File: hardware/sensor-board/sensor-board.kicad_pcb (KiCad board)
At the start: 2 copper layers, 65 x 76 mm, 76 parts, among them J1 HELM, J2 TACH, J3 PROBES, J4 RPi GPIO, J5 NMEA 2000, J6 LIGHTS, U1 ADS1115IDGSR, U2 ADS1115IDGSR, U3 EL817, U4 MCP2518FD, U5 ISO1044BD, U6 UA78L05, Y1 40MHz

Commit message: Sensor board: 5 V input (J7) that powers the Pi through the header
The Pi now runs from an external 12 V -> 5 V converter wired to J7 on the
board, through the header's 5 V pins (back-powering, 5 V +/-5 %, up to
2.5 A per the HAT guide); the board's 3V3 comes from the Pi as before.

An ideal diode sits in the way (TI LM74700-Q1 driving an IRLML0030): about
20 mV drop where a Schottky's 0.4 V would trip the Pi's undervoltage
warning. J7 wired backwards is blocked, and the Pi's USB-C can't push
current back into the converter. SMAJ5.0A clamp and 22 uF bulk on the
rail. Not protected: a converter failing with 12 V out (docs say to buy
one with output OVP).

The Pi's 5 V pins are in the header's top-left corner, boxed in by J1 and
a mounting hole, so J7 and the ideal diode go on a 35 x 12 mm tab above
the left half of the header (board now 65 x 88 overall). The router takes
an origin and off-board notches for that. Also:
- the 5 V current path routes wide first, sense pins and caps thin after;
  its run to the header goes on the bottom layer, where on top it walled
  off the header's GND pin 6 from the pour;
- vias keep their drill 0.25 mm off their own net's SMD pads (the router
  had put one on Q1's drain pad); none on the board now;
- BAT+ is documented as the dashboard switch's 12 V, the converter's feed.

ERC, DRC and parity: clean.

Co-Authored-By: Claude Opus 5.5 <noreply@anthropic.com>
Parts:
- added C19: 100n, sensor-board:C_0805_2012Metric_NoSilk, F.Cu at (126.6, 41.8)
- added C20: 100n, sensor-board:C_0805_2012Metric_NoSilk, F.Cu at (126.9, 45.4)
- added C21: 22u, sensor-board:C_1206_3216Metric_NoSilk, F.Cu at (129.6, 47.4)
- added D12: SMAJ5.0A, Diode_SMD:D_SMA, F.Cu at (132.6, 44.0)
- added J7: 5V IN, Connector_Phoenix_MC:PhoenixContact_MC_1,5_2-GF-3.81_1x02_P3.81mm_Horizontal_ThreadedFlange, F.Cu at (112.6, 46.7)
- added Q1: IRLML0030, Package_TO_SOT_SMD:SOT-23, F.Cu at (122.6, 47.8)
- added U7: LM74700-Q1, Package_TO_SOT_SMD:SOT-23-6, F.Cu at (122.7, 42.8)
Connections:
- J4 pad 2: unconnected-(J4-Pin_2-Pad2) -> +5V
- J4 pad 4: unconnected-(J4-Pin_4-Pad4) -> +5V
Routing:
- net +5V: track 0.00 -> 24.1 mm, vias 0 -> 1
- net /VIN: track 0.00 -> 23.8 mm
- net /N2K_GND: track 23.1 -> 32.3 mm, vias 2 -> 0
- net +3V3: track 190.5 -> 198.2 mm, vias 21 -> 19
- net /IDEAL_G: track 0.00 -> 3.77 mm, vias 0 -> 2
- net /N2K_L: track 19.7 -> 23.2 mm, vias 7 -> 6
- net GND: track 19.2 -> 21.3 mm, vias 36 -> 40
- net /N2K_H: track 26.7 -> 28.4 mm
- net /VCAP: track 0.00 -> 1.30 mm
- net /N2K_TERM: track 5.06 -> 6.19 mm, vias 0 -> 2
- net /LIGHT_DAT1: track 63.5 -> 64.5 mm
- net /CAN_INT: track 55.5 -> 56.5 mm
- net /LIGHT_DAT2: track 37.3 -> 38.3 mm
- net /N2K_5V: track 12.2 -> 13.0 mm
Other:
- board size 65 x 76 mm -> 65 x 88 mm
- board text added: "+5V"
- board text added: "5V IN: J7, converter at 5.1V"
- board text added: "BAT+: dashboard 12V, 1A fuse"
- board text added: "J7 5V IN"
- board text removed: "BAT+: +12V always on, 1A fuse"

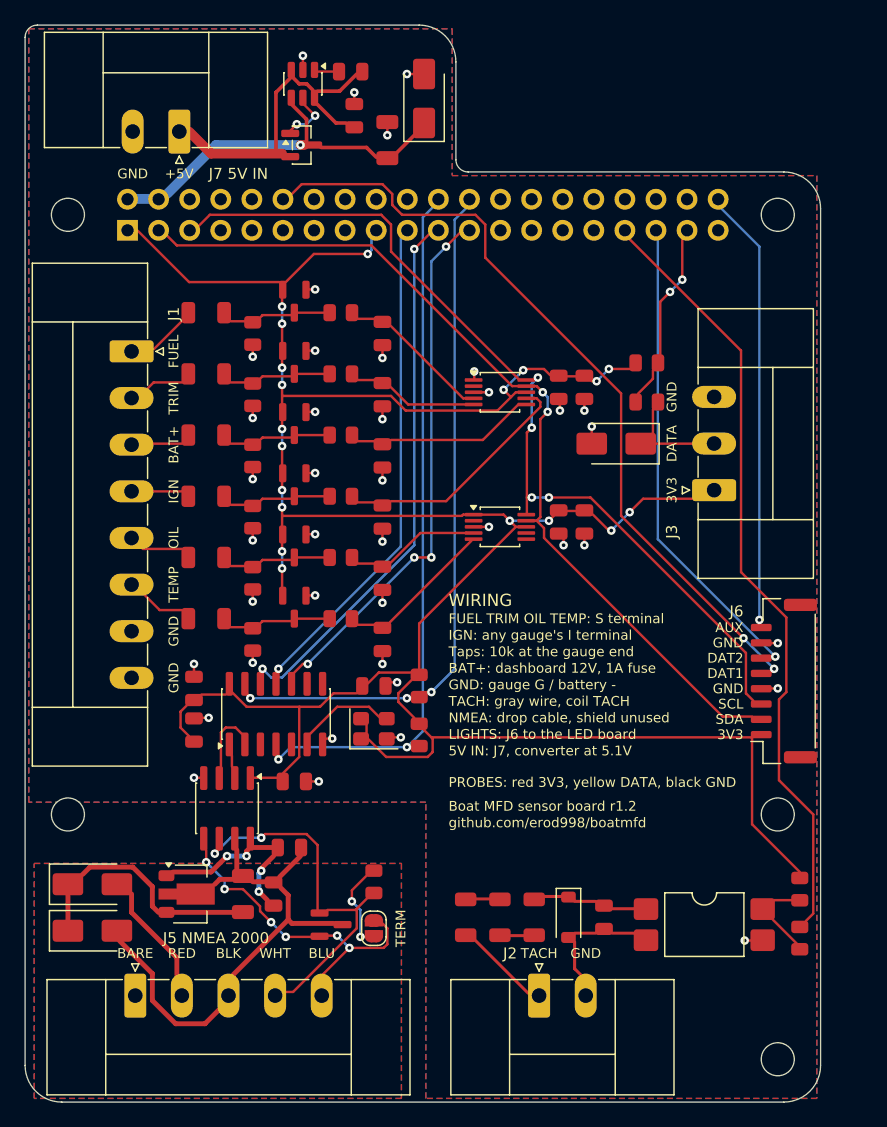
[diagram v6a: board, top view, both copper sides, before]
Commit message: Sensor board: no probe input; J6 gets its own I2C bus
No temperature probes on this boat: engine temperature comes from the temp
gauge's sender (J1 TEMP), water temperature from the depth transducer on
NMEA 2000. J3 and its 1-Wire parts (D8, R24, R25, GPIO26) are gone.

J6 moves to J3's old spot on the right edge, next to the header pins it
uses, and its SDA/SCL leave the converters' bus for a bus of their own:
i2c-gpio on GPIO5/6 (dtoverlay=i2c-gpio,bus=7,...; BOAT_LED_I2C_BUS=7),
4.7k pull-ups on the board (R24, R25). A stuck or shorted LED board can't
stall the engine data, and a bit-banged bus handles clock stretching,
which a microcontroller on the LED board may do and the Pi's hardware I2C
gets wrong. No hardware I2C pair is free at that corner of the header.

Routing: other nets now stay out of the half-pitch square round each of
the header's GND pins, on both layers. Tracks squeezed past them kept
starving their thermal spokes (pins 6, 14, 20, 25, 30, 34, 39 in turn);
this ends it for good.

SENSOR_BOARD.md says what J6 is enough for: PCA9685s at 16 PWM channels
each (four RGBW strips per chip, up to 62 chips), two independent
addressable data lines, and an RP2040 on the LED board for more.
The LED PWM driver opens BOAT_LED_I2C_BUS (defaults to BOAT_I2C_BUS).
Calibration page hides the probe card on the sensor board unless one
appears.

541 tests pass. ERC, DRC and parity: clean.

Co-Authored-By: Claude Opus 5.5 <noreply@anthropic.com>
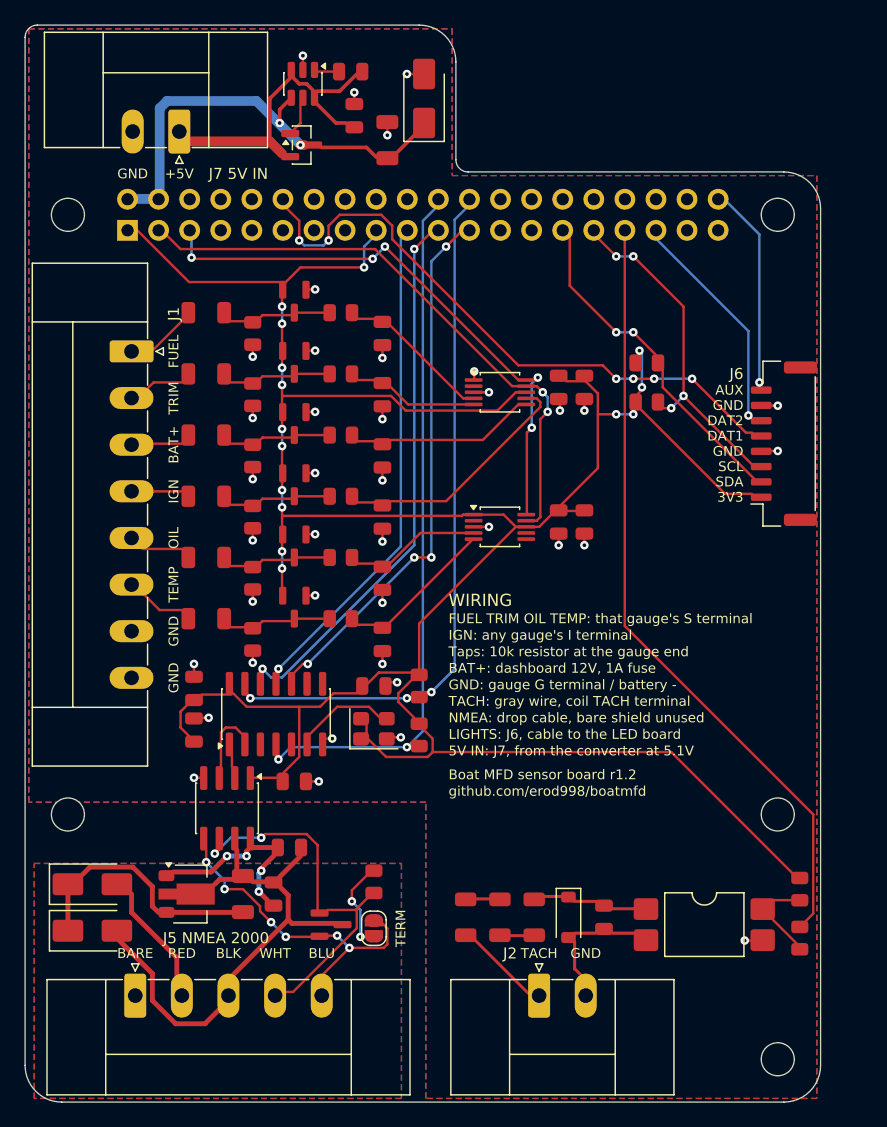
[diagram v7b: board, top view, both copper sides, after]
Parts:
- removed D8: SMAJ5.0A, Diode_SMD:D_SMA
- removed J3: PROBES, Connector_Phoenix_MC:PhoenixContact_MC_1,5_3-GF-3.81_1x03_P3.81mm_Horizontal_ThreadedFlange
- R25: value 100 -> 4.7k
- moved J6 19.4 mm to (162.0, 72.2)
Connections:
- J4 pad 29: unconnected-(J4-Pin_29-Pad29) -> /LIGHT_SDA
- J4 pad 31: unconnected-(J4-Pin_31-Pad31) -> /LIGHT_SCL
- J4 pad 37: /OW -> unconnected-(J4-Pin_37-Pad37)
- J6 pad 2: /SDA -> /LIGHT_SDA
- J6 pad 3: /SCL -> /LIGHT_SCL
- R24 pad 1: /OW -> /LIGHT_SDA
- R25 pad 1: /OW_EXT -> /LIGHT_SCL
- R25 pad 2: /OW -> +3V3
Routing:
- net /SCL: track 72.4 -> 44.9 mm, vias 4 -> 5
- net /LIGHT_SCL: track 0.00 -> 26.4 mm, vias 0 -> 4
- net /LIGHT_SDA: track 0.00 -> 25.2 mm, vias 0 -> 2
- net /SDA: track 70.6 -> 45.9 mm
- net /LIGHT_DAT2: track 38.3 -> 17.7 mm
- net /LIGHT_AUX: track 35.3 -> 16.2 mm
- net /LIGHT_DAT1: track 64.5 -> 49.9 mm, vias 2 -> 6
- net /OW: track 12.5 -> 0.00 mm, vias 2 -> 0
- net +3V3: track 198.2 -> 205.7 mm, vias 19 -> 15
- net +5V: track 24.1 -> 30.0 mm, vias 1 -> 2
- net /OW_EXT: track 5.00 -> 0.00 mm
- net /IDEAL_G: track 3.77 -> 2.35 mm, vias 2 -> 0
- net /VIN: track 23.8 -> 22.6 mm
- net GND: track 21.3 -> 20.8 mm, vias 40 -> 39
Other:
- board text added: "5V IN: J7, from the converter at 5.1V"
- board text added: "FUEL TRIM OIL TEMP: that gauge's S terminal"
- board text added: "GND: gauge G terminal / battery -"
- board text added: "LIGHTS: J6, cable to the LED board"
- board text added: "NMEA: drop cable, bare shield unused"
- board text added: "TACH: gray wire, coil TACH terminal"
- board text added: "Taps: 10k resistor at the gauge end"
- board text removed: "5V IN: J7, converter at 5.1V"
- board text removed: "DATA"
- board text removed: "FUEL TRIM OIL TEMP: S terminal"
- board text removed: "GND: gauge G / battery -"
- board text removed: "J3"
- board text removed: "LIGHTS: J6 to the LED board"
- board text removed: "NMEA: drop cable, shield unused"
- board text removed: "PROBES: red 3V3, yellow DATA, black GND"
- board text removed: "TACH: gray wire, coil TACH"
- board text removed: "Taps: 10k at the gauge end"

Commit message: Sensor board: tap resistors all on the board, plain wire to the gauges
Each tap's top resistor is now a single 49.9k 1% 1206 on the board
(R1, R2, R4-R6), in place of 39k here plus a 10k soldered into the tap
wire at the gauge end. The tap wires are plain wire from the gauge
terminals to J1; nothing to solder into the harness.

The trade-off, at the owner's call: a tap wire is now part of its gauge's
circuit, so one chafed to ground would read like a shorted sender on that
gauge (and on IGN would short the key-on 12 V). SENSOR_BOARD.md says so
and says to route and secure them accordingly.

BOAT_TAP_R_TOP defaults to 49900 (49000 for a rev 1.0-1.1 board). The
tap levels are ratios, so the setting only moves the gauge-supply volts.
Legend, schematic notes, BOM, wiring steps, bring-up and order sheet
updated; the gauge-end resistors are off the shopping list.

541 tests pass. ERC, DRC and parity: clean.

Co-Authored-By: Claude Opus 5.5 <noreply@anthropic.com>
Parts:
- R1, R2, R4, R5, R6: value 39k -> 49.9k
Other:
- board text removed: "Taps: 10k resistor at the gauge end"
